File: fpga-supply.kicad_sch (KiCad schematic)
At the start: 167 parts, among them U1 XC7K410T-2FFG900I

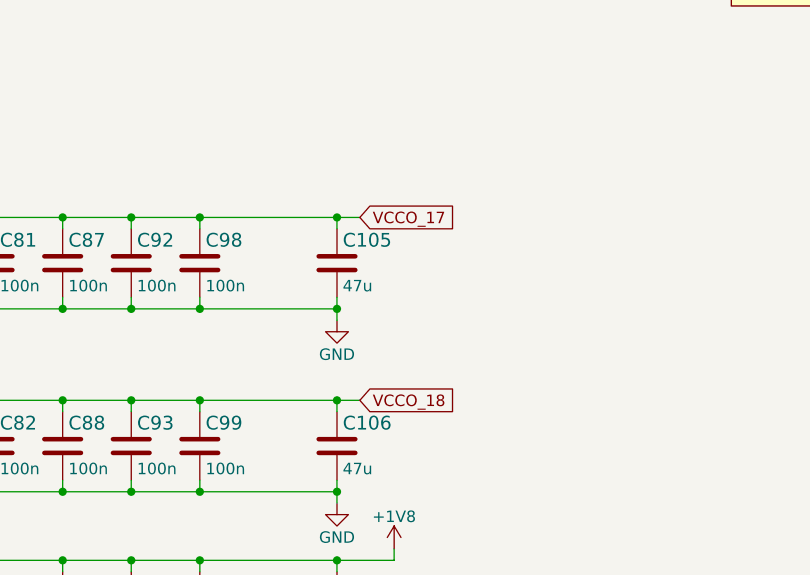
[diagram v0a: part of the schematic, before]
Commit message: Connect FPGA bank 17 and 18 to 3.3V
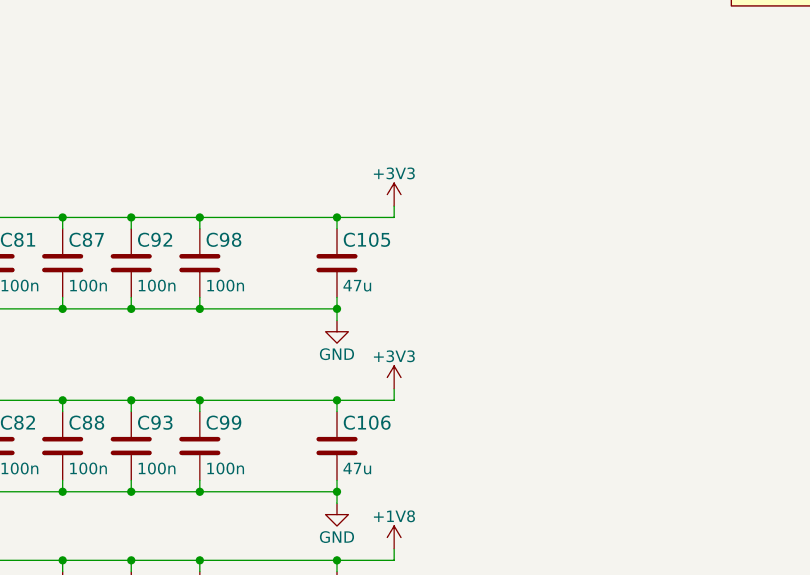
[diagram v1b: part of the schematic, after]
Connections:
- net VCCO_17 is gone; now on net +3V3: C105.1, C61.1, C67.1, C75.1, C81.1, C87.1, C92.1, C98.1, U1.A19 (VCCO_17), U1.B16 (VCCO_17), U1.D20 (VCCO_17), U1.E17 (VCCO_17), U1.G21 (VCCO_17), U1.H18 (VCCO_17), U1.L19 (VCCO_17)
- net VCCO_18 is gone; now on net +3V3: C106.1, C68.1, C76.1, C82.1, C88.1, C93.1, C99.1, U1.C13 (VCCO_18), U1.D10 (VCCO_18), U1.F14 (VCCO_18), U1.G11 (VCCO_18), U1.J15 (VCCO_18), U1.K12 (VCCO_18)
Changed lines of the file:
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@@
     (stroke (width 0) (type default) (color 0 0 0 0))
   )
+  (wire (pts (xy 208.915 206.375) (xy 208.915 207.645))
+    (stroke (width 0) (type default) (color 0 0 0 0))
+  )
   (wire (pts (xy 352.425 193.04) (xy 353.695 193.04))
     (stroke (width 0) (type default) (color 0 0 0 0))
@@
     (stroke (width 0) (type default) (color 0 0 0 0))
   )
+  (wire (pts (xy 208.915 186.055) (xy 208.915 187.325))
+    (stroke (width 0) (type default) (color 0 0 0 0))
+  )
   (wire (pts (xy 43.815 179.705) (xy 43.815 178.435))
     (stroke (width 0) (type default) (color 0 0 0 0))
@@
     (stroke (width 0) (type default) (color 0 0 0 0))
   )
-  (wire (pts (xy 205.105 207.645) (xy 202.565 207.645))
+  (wire (pts (xy 202.565 207.645) (xy 208.915 207.645))
     (stroke (width 0) (type default) (color 0 0 0 0))
   )
@@
     (stroke (width 0) (type default) (color 0 0 0 0))
   )
-  (wire (pts (xy 205.105 187.325) (xy 202.565 187.325))
+  (wire (pts (xy 202.565 187.325) (xy 208.915 187.325))
     (stroke (width 0) (type default) (color 0 0 0 0))
   )
@@
     )
   )
-  (global_label "VCCO_17" (shape input) (at 205.105 187.325 0) (fields_autoplaced)
-    (effects (font (size 1.27 1.27)) (justify left))
-    (property "Intersheet References" "${INTERSHEET_REFS}" (id 0) (at 215.8638 187.2456 0)
-      (effects (font (size 1.27 1.27)) (justify left) hide)
-    )
-  )
   (global_label "VCCUSERIOB" (shape input) (at 29.845 260.985 180) (fields_autoplaced)
     (effects (font (size 1.27 1.27)) (justify right))
@@
     )
   )
-  (global_label "VCCO_18" (shape input) (at 205.105 207.645 0) (fields_autoplaced)
-    (effects (font (size 1.27 1.27)) (justify left))
-    (property "Intersheet References" "${INTERSHEET_REFS}" (id 0) (at 215.8638 207.5656 0)
-      (effects (font (size 1.27 1.27)) (justify left) hide)
-    )
-  )
   (global_label "VCCUSERIOB" (shape input) (at 263.525 281.305 180) (fields_autoplaced)
     (effects (font (size 1.27 1.27)) (justify right))
@@
     (pin "2")
   )
+  (symbol (lib_id "power:+3V3") (at 208.915 186.055 0) (unit 1)
+    (in_bom yes) (on_board yes) (fields_autoplaced)
+    (property "Reference" "#PWR?" (id 0) (at 208.915 189.865 0)
+      (effects (font (size 1.27 1.27)) hide)
+    )
+    (property "Value" "+3V3" (id 1) (at 208.915 182.4792 0))
+    (property "Footprint" "" (id 2) (at 208.915 186.055 0)
+      (effects (font (size 1.27 1.27)) hide)
+    )
+    (property "Datasheet" "" (id 3) (at 208.915 186.055 0)
+      (effects (font (size 1.27 1.27)) hide)
+    )
+    (pin "1")
+  )
   (symbol (lib_id "power:GND") (at 32.385 201.295 0) (unit 1)
     (in_bom yes) (on_board yes)
@@
     (pin "2")
   )
+  (symbol (lib_id "power:+3V3") (at 208.915 206.375 0) (unit 1)
+    (in_bom yes) (on_board yes) (fields_autoplaced)
+    (property "Reference" "#PWR?" (id 0) (at 208.915 210.185 0)
+      (effects (font (size 1.27 1.27)) hide)
+    )
+    (property "Value" "+3V3" (id 1) (at 208.915 202.7992 0))
+    (property "Footprint" "" (id 2) (at 208.915 206.375 0)
+      (effects (font (size 1.27 1.27)) hide)
+    )
+    (property "Datasheet" "" (id 3) (at 208.915 206.375 0)
+      (effects (font (size 1.27 1.27)) hide)
+    )
+    (pin "1")
+  )
   (symbol (lib_id "antmicroCapacitors0402:C_4u7_0402") (at 83.82 69.85 0) (unit 1)

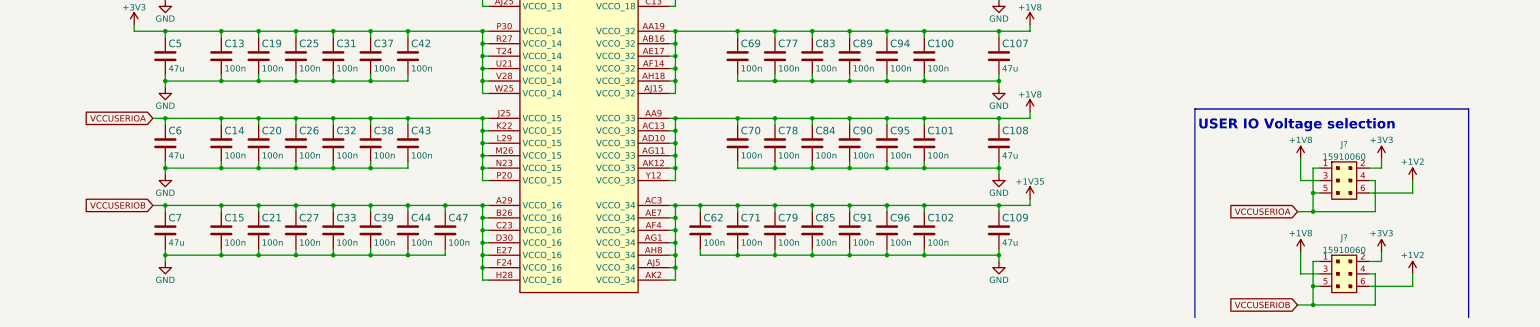
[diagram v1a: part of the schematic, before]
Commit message: Add VCC_USC_A/B labels, apply them to GPIO, FPGA power and SPI Flash
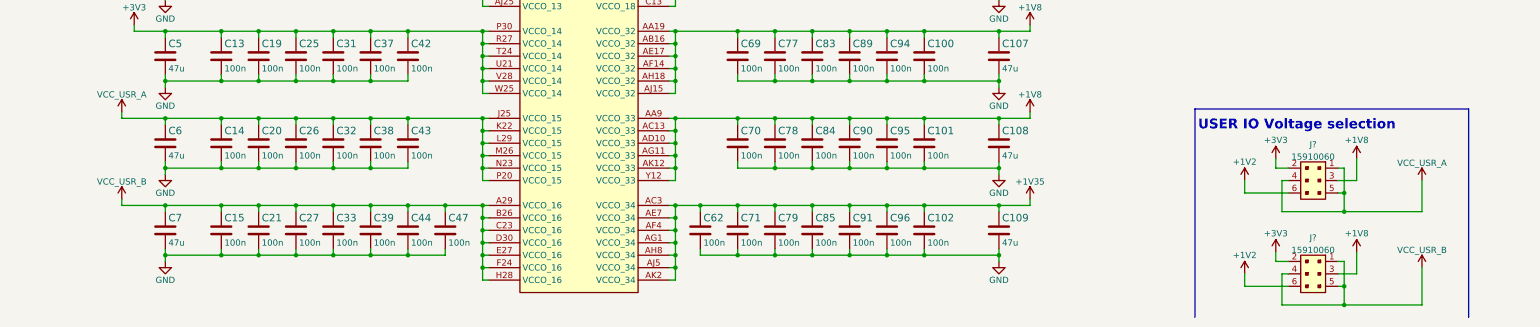
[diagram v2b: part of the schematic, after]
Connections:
- net VCCUSERIOA renamed VCC_USR_A
- net VCCUSERIOB renamed VCC_USR_B
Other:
- moved on the sheet: J?

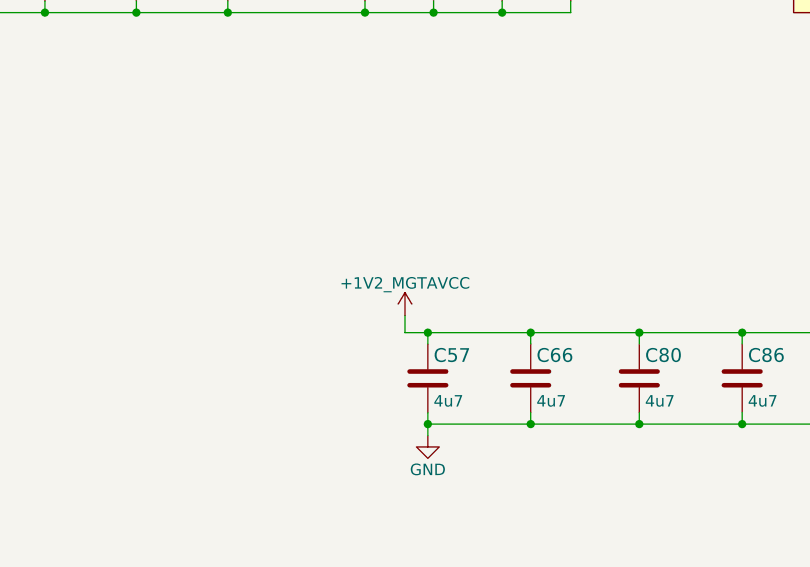
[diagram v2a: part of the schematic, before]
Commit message: Fix MGAVTT label
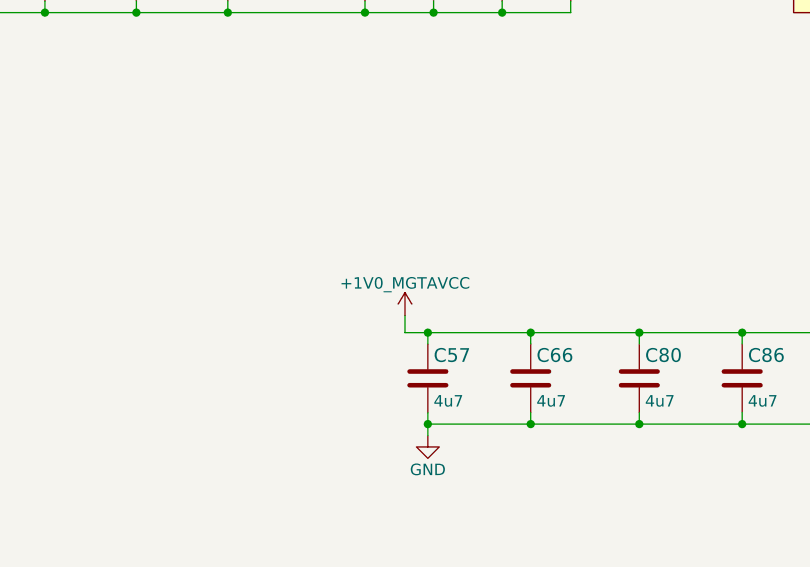
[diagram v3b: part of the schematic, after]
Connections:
- net +1V2_MGTAVCC renamed +1V0_MGTAVCC
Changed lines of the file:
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@@
     (pin "2")
+  )
+  (symbol (lib_id "antmicroPower:+1V0_MGTAVCC") (at 133.985 108.585 0) (unit 1)
+    (in_bom yes) (on_board yes) (fields_autoplaced)
+    (property "Reference" "#PWR?" (id 0) (at 133.985 112.395 0)
+      (effects (font (size 1.27 1.27)) hide)
+    )
+    (property "Value" "+1V0_MGTAVCC" (id 1) (at 133.985 105.0092 0))
+    (property "Footprint" "" (id 2) (at 133.985 108.585 0)
+      (effects (font (size 1.27 1.27)) hide)
+    )
+    (property "Datasheet" "" (id 3) (at 133.985 108.585 0)
+      (effects (font (size 1.27 1.27)) hide)
+    )
+    (pin "1")
   )
   (symbol (lib_id "antmicroCapacitorsmisc:C_100n_0201") (at 245.11 48.26 0) (unit 1)
@@
     (pin "2")
   )
-  (symbol (lib_id "antmicroPower:+1V2_MGTAVCC") (at 133.985 108.585 0) (unit 1)
-    (in_bom yes) (on_board yes) (fields_autoplaced)
-    (property "Reference" "#PWR017" (id 0) (at 133.985 112.395 0)
-      (effects (font (size 1.27 1.27)) hide)
-    )
-    (property "Value" "+1V2_MGTAVCC" (id 1) (at 133.985 105.0092 0))
-    (property "Footprint" "" (id 2) (at 133.985 108.585 0)
-      (effects (font (size 1.27 1.27)) hide)
-    )
-    (property "Datasheet" "" (id 3) (at 133.985 108.585 0)
-      (effects (font (size 1.27 1.27)) hide)
-    )
-    (pin "1")
-  )
   (symbol (lib_id "antmicroCapacitors0402:C_4u7_0402") (at 359.41 115.57 0) (mirror y) (unit 1)

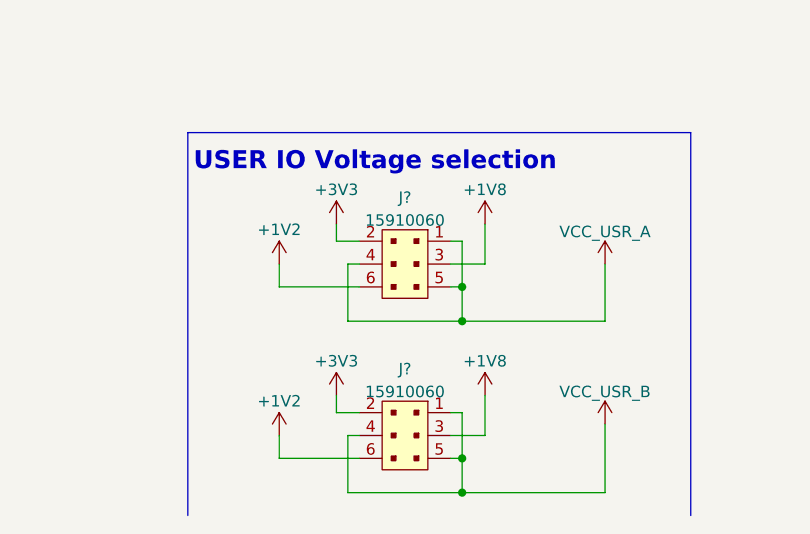
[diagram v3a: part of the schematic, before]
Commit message: Annotate new parts, sync schematic and PCB
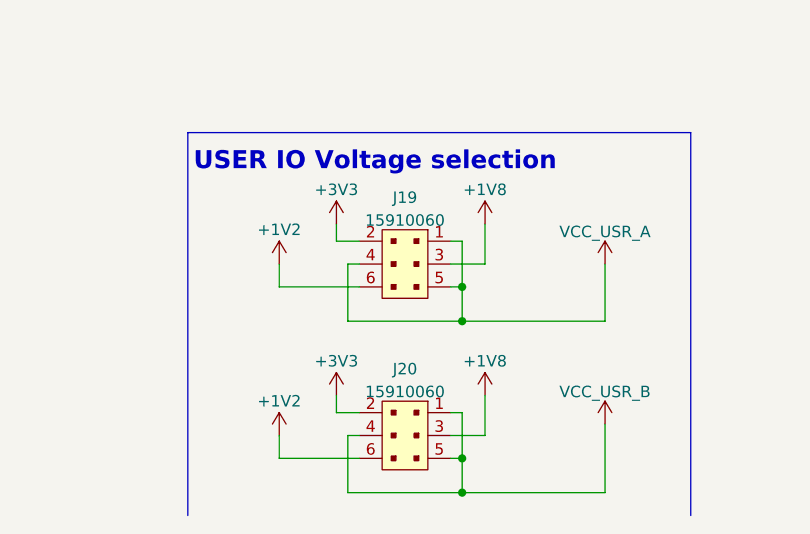
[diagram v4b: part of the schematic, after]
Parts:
- gave numbers to parts that had none: 2
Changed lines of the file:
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@@
   (symbol (lib_id "antmicroPower:VCC_USR_A") (at 288.925 255.905 0) (mirror y) (unit 1)
     (in_bom yes) (on_board yes) (fields_autoplaced)
-    (property "Reference" "#PWR?" (id 0) (at 288.925 259.715 0)
+    (property "Reference" "#PWR0429" (id 0) (at 288.925 259.715 0)
       (effects (font (size 1.27 1.27)) hide)
     )
@@
   (symbol (lib_id "power:+3V3") (at 208.915 186.055 0) (unit 1)
     (in_bom yes) (on_board yes) (fields_autoplaced)
-    (property "Reference" "#PWR?" (id 0) (at 208.915 189.865 0)
+    (property "Reference" "#PWR0437" (id 0) (at 208.915 189.865 0)
       (effects (font (size 1.27 1.27)) hide)
     )
@@
   (symbol (lib_id "antmicroRectangularConnectorsHeadersMalePins:15910060") (at 266.7 274.955 0) (mirror y) (unit 1)
     (in_bom yes) (on_board yes) (fields_autoplaced)
-    (property "Reference" "J?" (id 0) (at 266.7 267.5722 0))
+    (property "Reference" "J20" (id 0) (at 266.7 267.5722 0))
     (property "Value" "15910060" (id 1) (at 266.7 270.1091 0))
     (property "Footprint" "antmicro-footprints:15910060" (id 2) (at 284.48 287.655 0)
@@
   (symbol (lib_id "power:+1V2") (at 252.73 274.955 0) (mirror y) (unit 1)
     (in_bom yes) (on_board yes)
-    (property "Reference" "#PWR?" (id 0) (at 252.73 278.765 0)
+    (property "Reference" "#PWR0431" (id 0) (at 252.73 278.765 0)
       (effects (font (size 1.27 1.27)) hide)
     )
@@
   (symbol (lib_id "power:+3V3") (at 259.08 270.51 0) (mirror y) (unit 1)
     (in_bom yes) (on_board yes)
-    (property "Reference" "#PWR?" (id 0) (at 259.08 274.32 0)
+    (property "Reference" "#PWR0435" (id 0) (at 259.08 274.32 0)
       (effects (font (size 1.27 1.27)) hide)
     )
@@
   (symbol (lib_id "antmicroPower:+1V0_MGTAVCC") (at 133.985 108.585 0) (unit 1)
     (in_bom yes) (on_board yes) (fields_autoplaced)
-    (property "Reference" "#PWR?" (id 0) (at 133.985 112.395 0)
+    (property "Reference" "#PWR0439" (id 0) (at 133.985 112.395 0)
       (effects (font (size 1.27 1.27)) hide)
     )
@@
   (symbol (lib_id "power:+1V8") (at 275.59 251.46 0) (mirror y) (unit 1)
     (in_bom yes) (on_board yes)
-    (property "Reference" "#PWR?" (id 0) (at 275.59 255.27 0)
+    (property "Reference" "#PWR0427" (id 0) (at 275.59 255.27 0)
       (effects (font (size 1.27 1.27)) hide)
     )
@@
   (symbol (lib_id "antmicroRectangularConnectorsHeadersMalePins:15910060") (at 266.7 255.905 0) (mirror y) (unit 1)
     (in_bom yes) (on_board yes) (fields_autoplaced)
-    (property "Reference" "J?" (id 0) (at 266.7 248.5222 0))
+    (property "Reference" "J19" (id 0) (at 266.7 248.5222 0))
     (property "Value" "15910060" (id 1) (at 266.7 251.0591 0))
     (property "Footprint" "antmicro-footprints:15910060" (id 2) (at 284.48 268.605 0)
@@
   (symbol (lib_id "antmicroPower:VCC_USR_B") (at 23.495 259.715 0) (unit 1)
     (in_bom yes) (on_board yes) (fields_autoplaced)
-    (property "Reference" "#PWR?" (id 0) (at 23.495 263.525 0)
+    (property "Reference" "#PWR0441" (id 0) (at 23.495 263.525 0)
       (effects (font (size 1.27 1.27)) hide)
     )
@@
   (symbol (lib_id "power:+1V2") (at 252.73 255.905 0) (mirror y) (unit 1)
     (in_bom yes) (on_board yes)
-    (property "Reference" "#PWR?" (id 0) (at 252.73 259.715 0)
+    (property "Reference" "#PWR0356" (id 0) (at 252.73 259.715 0)
       (effects (font (size 1.27 1.27)) hide)
     )
@@
   (symbol (lib_id "antmicroPower:VCC_USR_B") (at 288.925 273.685 0) (mirror y) (unit 1)
     (in_bom yes) (on_board yes) (fields_autoplaced)
-    (property "Reference" "#PWR?" (id 0) (at 288.925 277.495 0)
+    (property "Reference" "#PWR0430" (id 0) (at 288.925 277.495 0)
       (effects (font (size 1.27 1.27)) hide)
     )
@@
   (symbol (lib_id "power:+1V8") (at 275.59 270.51 0) (mirror y) (unit 1)
     (in_bom yes) (on_board yes)
-    (property "Reference" "#PWR?" (id 0) (at 275.59 274.32 0)
+    (property "Reference" "#PWR0428" (id 0) (at 275.59 274.32 0)
       (effects (font (size 1.27 1.27)) hide)
     )
@@
   (symbol (lib_id "power:+3V3") (at 208.915 206.375 0) (unit 1)
     (in_bom yes) (on_board yes) (fields_autoplaced)
-    (property "Reference" "#PWR?" (id 0) (at 208.915 210.185 0)
+    (property "Reference" "#PWR0438" (id 0) (at 208.915 210.185 0)
       (effects (font (size 1.27 1.27)) hide)
     )
@@
   (symbol (lib_id "power:+3V3") (at 259.08 251.46 0) (mirror y) (unit 1)
     (in_bom yes) (on_board yes)
-    (property "Reference" "#PWR?" (id 0) (at 259.08 255.27 0)
+    (property "Reference" "#PWR0381" (id 0) (at 259.08 255.27 0)
       (effects (font (size 1.27 1.27)) hide)
     )
@@
   (symbol (lib_id "antmicroPower:VCC_USR_A") (at 23.495 241.935 0) (unit 1)
     (in_bom yes) (on_board yes) (fields_autoplaced)
-    (property "Reference" "#PWR?" (id 0) (at 23.495 245.745 0)
+    (property "Reference" "#PWR0440" (id 0) (at 23.495 245.745 0)
       (effects (font (size 1.27 1.27)) hide)
     )
